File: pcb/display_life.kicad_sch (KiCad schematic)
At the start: 45 parts, among them J3 1st Bit_shifter, J4 1st 7 Segment, Q1 Q_NPN_CBE, Q2 Q_NPN_CBE, Q3 Q_NPN_CBE, Q4 Q_NPN_CBE, Q5 Q_NPN_CBE, Q6 Q_NPN_CBE, Q7 Q_NPN_CBE, Q8 Q_NPN_CBE, U2 74HC595, U3 74HC595, U4 4028, U5 CC56-12SURKWA, U6 CC56-12SURKWA

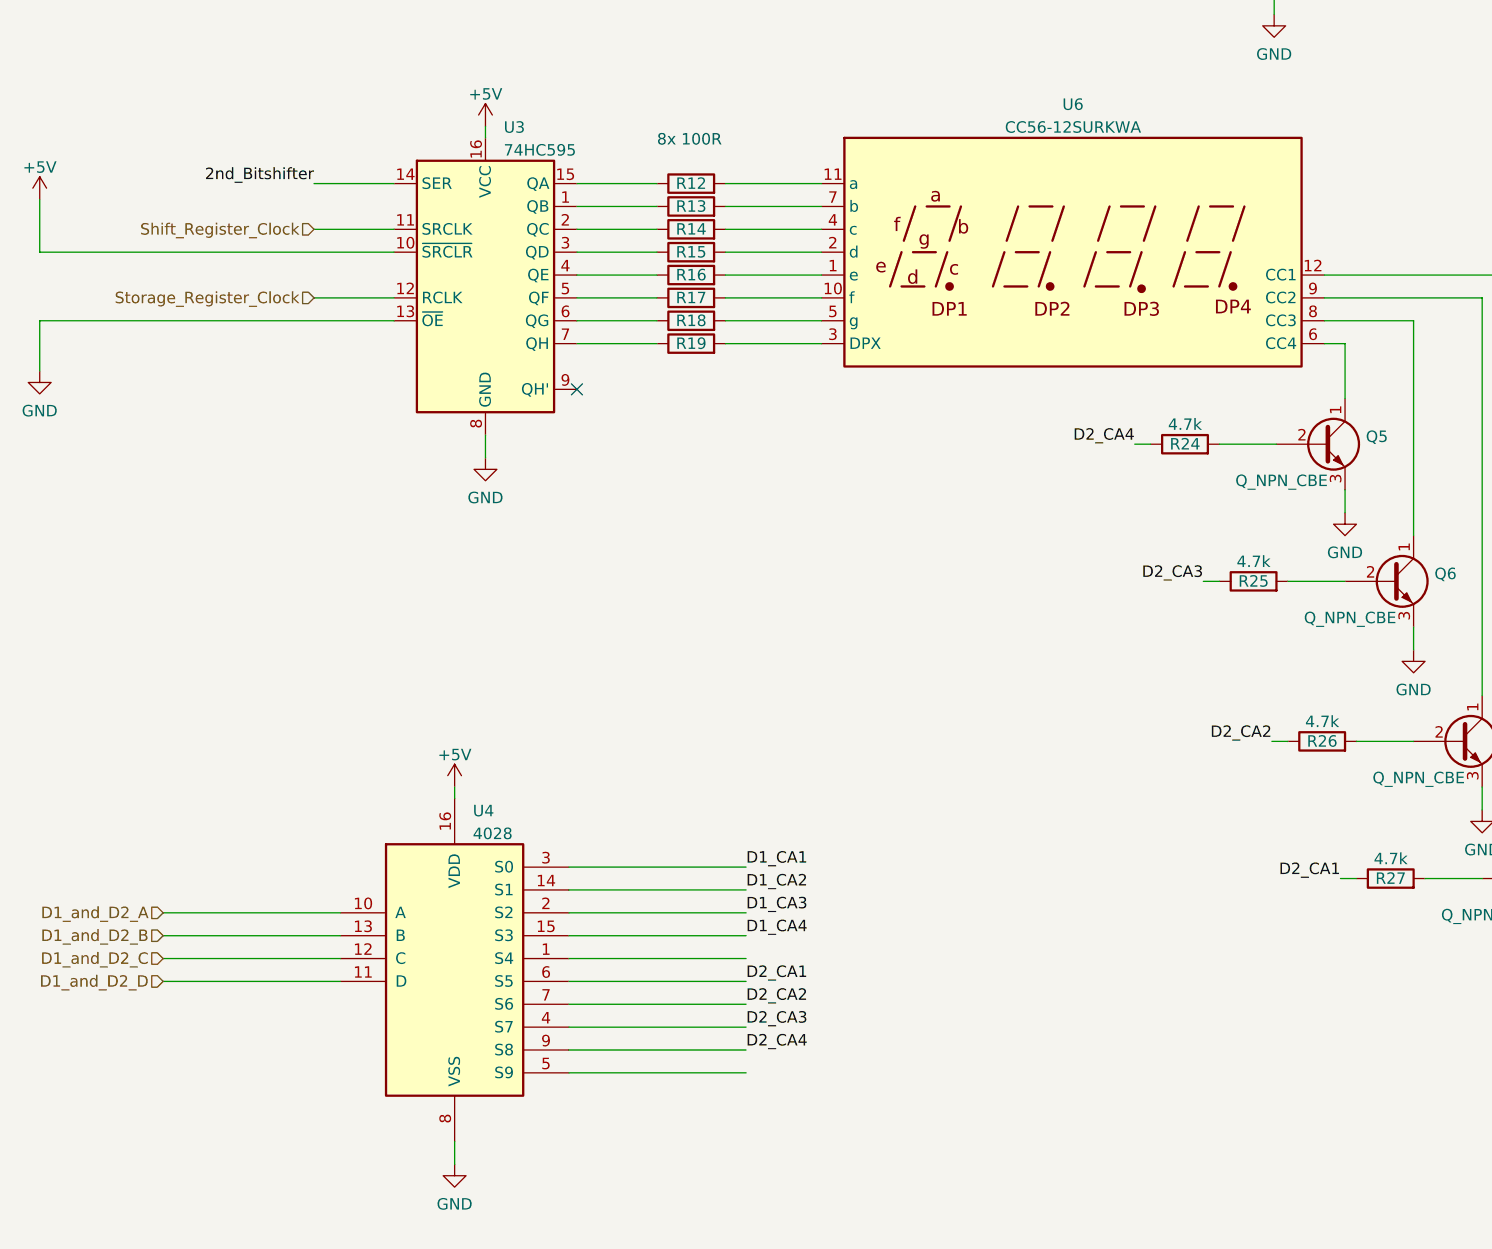
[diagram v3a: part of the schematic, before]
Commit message: reduced to 2 displays and logig analyzer output added
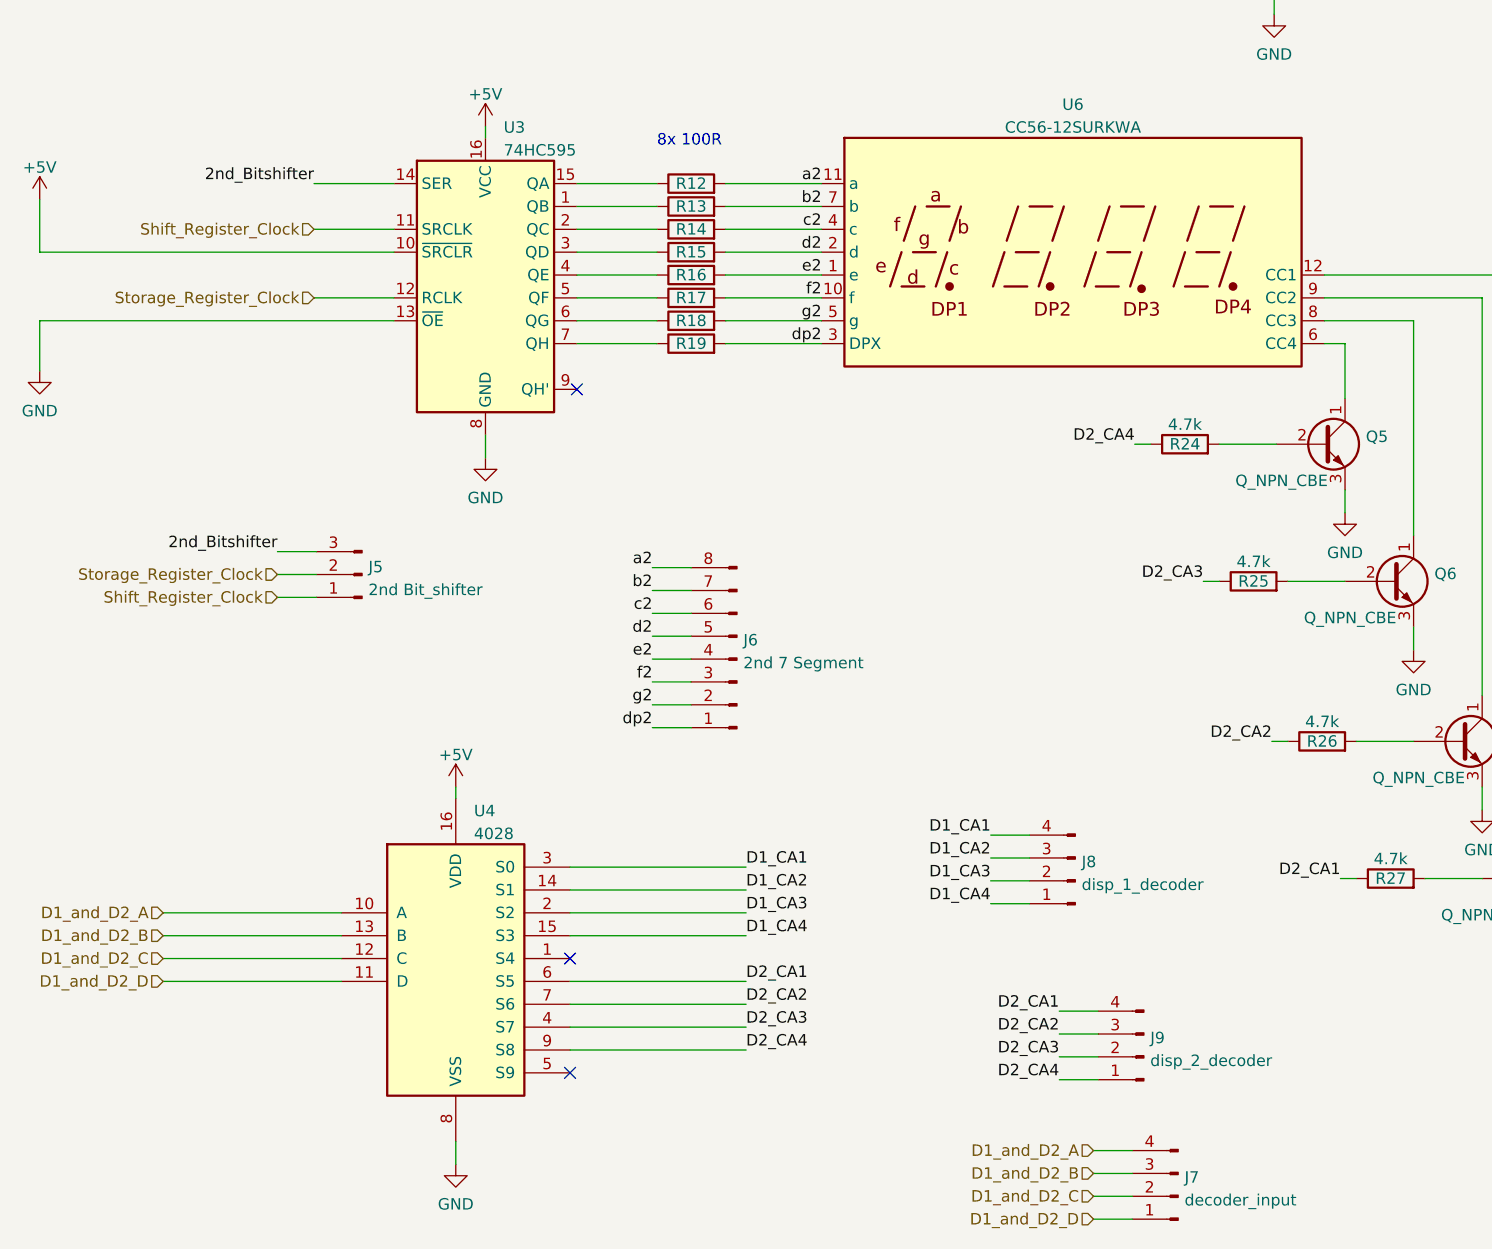
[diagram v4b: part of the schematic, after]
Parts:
- added J5: 2nd Bit_shifter, Connector_PinHeader_2.54mm:PinHeader_1x03_P2.54mm_Vertical, symbol Connector:Conn_01x03_Male
- added J6: 2nd 7 Segment, Connector_PinHeader_2.54mm:PinHeader_1x08_P2.54mm_Vertical, symbol Connector:Conn_01x08_Male
- added J7: decoder_input, Connector_PinHeader_2.54mm:PinHeader_1x04_P2.54mm_Vertical, symbol Connector:Conn_01x04_Male
- added J8: disp_1_decoder, Connector_PinHeader_2.54mm:PinHeader_1x04_P2.54mm_Vertical, symbol Connector:Conn_01x04_Male
- added J9: disp_2_decoder, Connector_PinHeader_2.54mm:PinHeader_1x04_P2.54mm_Vertical, symbol Connector:Conn_01x04_Male
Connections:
- net 2nd_Bitshifter: now also J5.3 (Pin_3)
- net D1_CA1: now also J8.4 (Pin_4)
- net D1_CA2: now also J8.3 (Pin_3)
- net D1_CA3: now also J8.2 (Pin_2)
- net D1_CA4: now also J8.1 (Pin_1)
- net D1_and_D2_A: now also J7.4 (Pin_4)
- net D1_and_D2_B: now also J7.3 (Pin_3)
- net D1_and_D2_C: now also J7.2 (Pin_2)
- net D1_and_D2_D: now also J7.1 (Pin_1)
- net D2_CA1: now also J9.4 (Pin_4)
- net D2_CA2: now also J9.3 (Pin_3)
- net D2_CA3: now also J9.2 (Pin_2)
- net D2_CA4: now also J9.1 (Pin_1)
- net Shift_Register_Clock: now also J5.1 (Pin_1)
- net Storage_Register_Clock: now also J5.2 (Pin_2)
- net e2: now reaches R16.2, U6.1 (e)
- net e2: now also J6.4 (Pin_4)
- net c2: now reaches R14.2, U6.4 (c)
- net c2: now also J6.6 (Pin_6)
- net a2: now reaches R12.2, U6.11 (a)
- net a2: now also J6.8 (Pin_8)
- net b2: now reaches R13.2, U6.7 (b)
- net b2: now also J6.7 (Pin_7)
- net f2: now reaches R17.2, U6.10 (f)
- net f2: now also J6.3 (Pin_3)
- net d2: now reaches R15.2, U6.2 (d)
- net d2: now also J6.5 (Pin_5)
- net dp2: now reaches R19.2, U6.3 (DPX)
- net dp2: now also J6.1 (Pin_1)
- net g2: now reaches R18.2, U6.5 (g)
- net g2: now also J6.2 (Pin_2)
- no-connect marks 1 -> 3

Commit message: new parts and stuff
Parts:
- removed J4: 1st 7 Segment, Connector_PinHeader_2.54mm:PinHeader_1x08_P2.54mm_Vertical, symbol Connector:Conn_01x08_Male
- removed J6: 2nd 7 Segment, Connector_PinHeader_2.54mm:PinHeader_1x08_P2.54mm_Vertical, symbol Connector:Conn_01x08_Male
- added J4: 1st 7 Segment, Connector_PinHeader_2.54mm:PinHeader_1x10_P2.54mm_Vertical, symbol Connector:Conn_01x10_Female
- added J6: 2nd 7 Segment, Connector_PinHeader_2.54mm:PinHeader_1x10_P2.54mm_Vertical, symbol Connector:Conn_01x10_Female
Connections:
- net +5V: now also J4.1 (Pin_1), J6.1 (Pin_1)
- net GND: now also J4.10 (Pin_10), J6.10 (Pin_10)
- net a1: now also J4.2 (Pin_2)
- net a2: now also J6.2 (Pin_2)
- net b1: now also J4.3 (Pin_3)
- net b2: now also J6.3 (Pin_3)
- net c1: now also J4.4 (Pin_4)
- net c2: now also J6.4 (Pin_4)
- net d1: now also J4.5 (Pin_5)
- net d2: now also J6.5 (Pin_5)
- net dp1: now also J4.9 (Pin_9)
- net dp2: now also J6.9 (Pin_9)
- net e1: now also J4.6 (Pin_6)
- net e2: now also J6.6 (Pin_6)
- net f1: now also J4.7 (Pin_7)
- net f2: now also J6.7 (Pin_7)
- net g1: now also J4.8 (Pin_8)
- net g2: now also J6.8 (Pin_8)
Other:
- note added: "Debug Pins"
- moved on the sheet: J3, J5, J7, J8, J9, U4

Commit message: new layout with usb
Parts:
- R10, R11, R12, R13, R14, R15, R16, R17, R18, R19, R20, R21, R22, R23, R24, R25, R26, R27, R4, R5, R6, R7, R8, R9: footprint Resistor_THT:R_Axial_DIN0207_L6.3mm_D2.5mm_P7.62mm_Horizontal -> Resistor_THT:R_Axial_DIN0207_L6.3mm_D2.5mm_P10.16mm_Horizontal
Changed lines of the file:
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@@
       (effects (font (size 1.27 1.27)) hide)
     )
-    (property "Footprint" "Resistor_THT:R_Axial_DIN0207_L6.3mm_D2.5mm_P7.62mm_Horizontal" (id 2) (at 94.488 87.884 90)
+    (property "Footprint" "Resistor_THT:R_Axial_DIN0207_L6.3mm_D2.5mm_P10.16mm_Horizontal" (id 2) (at 94.488 87.884 90)
       (effects (font (size 1.27 1.27)) hide)
     )
@@
     (property "Reference" "R21" (id 0) (at 244.602 70.866 90))
     (property "Value" "4.7k" (id 1) (at 244.602 68.6871 90))
-    (property "Footprint" "Resistor_THT:R_Axial_DIN0207_L6.3mm_D2.5mm_P7.62mm_Horizontal" (id 2) (at 244.602 72.644 90)
+    (property "Footprint" "Resistor_THT:R_Axial_DIN0207_L6.3mm_D2.5mm_P10.16mm_Horizontal" (id 2) (at 244.602 72.644 90)
       (effects (font (size 1.27 1.27)) hide)
     )
@@
     (property "Reference" "R20" (id 0) (at 236.982 55.626 90))
     (property "Value" "4.7k" (id 1) (at 236.982 53.4471 90))
-    (property "Footprint" "Resistor_THT:R_Axial_DIN0207_L6.3mm_D2.5mm_P7.62mm_Horizontal" (id 2) (at 236.982 57.404 90)
+    (property "Footprint" "Resistor_THT:R_Axial_DIN0207_L6.3mm_D2.5mm_P10.16mm_Horizontal" (id 2) (at 236.982 57.404 90)
       (effects (font (size 1.27 1.27)) hide)
     )
@@
       (effects (font (size 1.27 1.27)) hide)
     )
-    (property "Footprint" "Resistor_THT:R_Axial_DIN0207_L6.3mm_D2.5mm_P7.62mm_Horizontal" (id 2) (at 94.488 82.804 90)
+    (property "Footprint" "Resistor_THT:R_Axial_DIN0207_L6.3mm_D2.5mm_P10.16mm_Horizontal" (id 2) (at 94.488 82.804 90)
       (effects (font (size 1.27 1.27)) hide)
     )
@@
     (property "Reference" "R24" (id 0) (at 149.352 104.902 90))
     (property "Value" "4.7k" (id 1) (at 149.352 102.7231 90))
-    (property "Footprint" "Resistor_THT:R_Axial_DIN0207_L6.3mm_D2.5mm_P7.62mm_Horizontal" (id 2) (at 149.352 106.68 90)
+    (property "Footprint" "Resistor_THT:R_Axial_DIN0207_L6.3mm_D2.5mm_P10.16mm_Horizontal" (id 2) (at 149.352 106.68 90)
       (effects (font (size 1.27 1.27)) hide)
     )
@@
       (effects (font (size 1.27 1.27)) hide)
     )
-    (property "Footprint" "Resistor_THT:R_Axial_DIN0207_L6.3mm_D2.5mm_P7.62mm_Horizontal" (id 2) (at 182.118 30.988 90)
+    (property "Footprint" "Resistor_THT:R_Axial_DIN0207_L6.3mm_D2.5mm_P10.16mm_Horizontal" (id 2) (at 182.118 30.988 90)
       (effects (font (size 1.27 1.27)) hide)
     )
@@
     (property "Reference" "R23" (id 0) (at 259.842 103.886 90))
     (property "Value" "4.7k" (id 1) (at 259.842 101.7071 90))
-    (property "Footprint" "Resistor_THT:R_Axial_DIN0207_L6.3mm_D2.5mm_P7.62mm_Horizontal" (id 2) (at 259.842 105.664 90)
+    (property "Footprint" "Resistor_THT:R_Axial_DIN0207_L6.3mm_D2.5mm_P10.16mm_Horizontal" (id 2) (at 259.842 105.664 90)
       (effects (font (size 1.27 1.27)) hide)
     )
@@
     (property "Reference" "R25" (id 0) (at 156.972 120.142 90))
     (property "Value" "4.7k" (id 1) (at 156.972 117.9631 90))
-    (property "Footprint" "Resistor_THT:R_Axial_DIN0207_L6.3mm_D2.5mm_P7.62mm_Horizontal" (id 2) (at 156.972 121.92 90)
+    (property "Footprint" "Resistor_THT:R_Axial_DIN0207_L6.3mm_D2.5mm_P10.16mm_Horizontal" (id 2) (at 156.972 121.92 90)
       (effects (font (size 1.27 1.27)) hide)
     )
@@
       (effects (font (size 1.27 1.27)) hide)
     )
-    (property "Footprint" "Resistor_THT:R_Axial_DIN0207_L6.3mm_D2.5mm_P7.62mm_Horizontal" (id 2) (at 182.118 46.228 90)
+    (property "Footprint" "Resistor_THT:R_Axial_DIN0207_L6.3mm_D2.5mm_P10.16mm_Horizontal" (id 2) (at 182.118 46.228 90)
       (effects (font (size 1.27 1.27)) hide)
     )
@@
     (property "Reference" "R26" (id 0) (at 164.592 137.922 90))
     (property "Value" "4.7k" (id 1) (at 164.592 135.7431 90))
-    (property "Footprint" "Resistor_THT:R_Axial_DIN0207_L6.3mm_D2.5mm_P7.62mm_Horizontal" (id 2) (at 164.592 139.7 90)
+    (property "Footprint" "Resistor_THT:R_Axial_DIN0207_L6.3mm_D2.5mm_P10.16mm_Horizontal" (id 2) (at 164.592 139.7 90)
       (effects (font (size 1.27 1.27)) hide)
     )
@@
       (effects (font (size 1.27 1.27)) hide)
     )
-    (property "Footprint" "Resistor_THT:R_Axial_DIN0207_L6.3mm_D2.5mm_P7.62mm_Horizontal" (id 2) (at 182.118 36.068 90)
+    (property "Footprint" "Resistor_THT:R_Axial_DIN0207_L6.3mm_D2.5mm_P10.16mm_Horizontal" (id 2) (at 182.118 36.068 90)
       (effects (font (size 1.27 1.27)) hide)
     )
@@
       (effects (font (size 1.27 1.27)) hide)
     )
-    (property "Footprint" "Resistor_THT:R_Axial_DIN0207_L6.3mm_D2.5mm_P7.62mm_Horizontal" (id 2) (at 94.488 77.724 90)
+    (property "Footprint" "Resistor_THT:R_Axial_DIN0207_L6.3mm_D2.5mm_P10.16mm_Horizontal" (id 2) (at 94.488 77.724 90)
       (effects (font (size 1.27 1.27)) hide)
     )
@@
       (effects (font (size 1.27 1.27)) hide)
     )
-    (property "Footprint" "Resistor_THT:R_Axial_DIN0207_L6.3mm_D2.5mm_P7.62mm_Horizontal" (id 2) (at 94.488 80.264 90)
+    (property "Footprint" "Resistor_THT:R_Axial_DIN0207_L6.3mm_D2.5mm_P10.16mm_Horizontal" (id 2) (at 94.488 80.264 90)
       (effects (font (size 1.27 1.27)) hide)
     )
@@
       (effects (font (size 1.27 1.27)) hide)
     )
-    (property "Footprint" "Resistor_THT:R_Axial_DIN0207_L6.3mm_D2.5mm_P7.62mm_Horizontal" (id 2) (at 94.488 90.424 90)
+    (property "Footprint" "Resistor_THT:R_Axial_DIN0207_L6.3mm_D2.5mm_P10.16mm_Horizontal" (id 2) (at 94.488 90.424 90)
       (effects (font (size 1.27 1.27)) hide)
     )
@@
       (effects (font (size 1.27 1.27)) hide)
     )
-    (property "Footprint" "Resistor_THT:R_Axial_DIN0207_L6.3mm_D2.5mm_P7.62mm_Horizontal" (id 2) (at 94.488 85.344 90)
+    (property "Footprint" "Resistor_THT:R_Axial_DIN0207_L6.3mm_D2.5mm_P10.16mm_Horizontal" (id 2) (at 94.488 85.344 90)
       (effects (font (size 1.27 1.27)) hide)
     )
@@
       (effects (font (size 1.27 1.27)) hide)
     )
-    (property "Footprint" "Resistor_THT:R_Axial_DIN0207_L6.3mm_D2.5mm_P7.62mm_Horizontal" (id 2) (at 182.118 41.148 90)
+    (property "Footprint" "Resistor_THT:R_Axial_DIN0207_L6.3mm_D2.5mm_P10.16mm_Horizontal" (id 2) (at 182.118 41.148 90)
       (effects (font (size 1.27 1.27)) hide)
     )
@@
       (effects (font (size 1.27 1.27)) hide)
     )
-    (property "Footprint" "Resistor_THT:R_Axial_DIN0207_L6.3mm_D2.5mm_P7.62mm_Horizontal" (id 2) (at 94.488 92.964 90)
+    (property "Footprint" "Resistor_THT:R_Axial_DIN0207_L6.3mm_D2.5mm_P10.16mm_Horizontal" (id 2) (at 94.488 92.964 90)
       (effects (font (size 1.27 1.27)) hide)
     )
@@
       (effects (font (size 1.27 1.27)) hide)
     )
-    (property "Footprint" "Resistor_THT:R_Axial_DIN0207_L6.3mm_D2.5mm_P7.62mm_Horizontal" (id 2) (at 182.118 28.448 90)
+    (property "Footprint" "Resistor_THT:R_Axial_DIN0207_L6.3mm_D2.5mm_P10.16mm_Horizontal" (id 2) (at 182.118 28.448 90)
       (effects (font (size 1.27 1.27)) hide)
     )
@@
       (effects (font (size 1.27 1.27)) hide)
     )
-    (property "Footprint" "Resistor_THT:R_Axial_DIN0207_L6.3mm_D2.5mm_P7.62mm_Horizontal" (id 2) (at 182.118 38.608 90)
+    (property "Footprint" "Resistor_THT:R_Axial_DIN0207_L6.3mm_D2.5mm_P10.16mm_Horizontal" (id 2) (at 182.118 38.608 90)
       (effects (font (size 1.27 1.27)) hide)
     )
@@
       (effects (font (size 1.27 1.27)) hide)
     )
-    (property "Footprint" "Resistor_THT:R_Axial_DIN0207_L6.3mm_D2.5mm_P7.62mm_Horizontal" (id 2) (at 182.118 43.688 90)
+    (property "Footprint" "Resistor_THT:R_Axial_DIN0207_L6.3mm_D2.5mm_P10.16mm_Horizontal" (id 2) (at 182.118 43.688 90)
       (effects (font (size 1.27 1.27)) hide)
     )
@@
       (effects (font (size 1.27 1.27)) hide)
     )
-    (property "Footprint" "Resistor_THT:R_Axial_DIN0207_L6.3mm_D2.5mm_P7.62mm_Horizontal" (id 2) (at 182.118 33.528 90)
+    (property "Footprint" "Resistor_THT:R_Axial_DIN0207_L6.3mm_D2.5mm_P10.16mm_Horizontal" (id 2) (at 182.118 33.528 90)
       (effects (font (size 1.27 1.27)) hide)
     )
@@
     (property "Reference" "R27" (id 0) (at 172.212 153.162 90))
     (property "Value" "4.7k" (id 1) (at 172.212 150.9831 90))
-    (property "Footprint" "Resistor_THT:R_Axial_DIN0207_L6.3mm_D2.5mm_P7.62mm_Horizontal" (id 2) (at 172.212 154.94 90)
+    (property "Footprint" "Resistor_THT:R_Axial_DIN0207_L6.3mm_D2.5mm_P10.16mm_Horizontal" (id 2) (at 172.212 154.94 90)
       (effects (font (size 1.27 1.27)) hide)
     )
@@
       (effects (font (size 1.27 1.27)) hide)
     )
-    (property "Footprint" "Resistor_THT:R_Axial_DIN0207_L6.3mm_D2.5mm_P7.62mm_Horizontal" (id 2) (at 94.488 95.504 90)
+    (property "Footprint" "Resistor_THT:R_Axial_DIN0207_L6.3mm_D2.5mm_P10.16mm_Horizontal" (id 2) (at 94.488 95.504 90)
       (effects (font (size 1.27 1.27)) hide)
     )
@@
     (property "Reference" "R22" (id 0) (at 252.222 88.646 90))
     (property "Value" "4.7k" (id 1) (at 252.222 86.4671 90))
-    (property "Footprint" "Resistor_THT:R_Axial_DIN0207_L6.3mm_D2.5mm_P7.62mm_Horizontal" (id 2) (at 252.222 90.424 90)
-      (effects (font (size 1.27 1.27)) hide)
-    )
+    (property "Footprint" "Resistor_THT:R_Axial_DIN0207_L6.3mm_D2.5mm_P10.16mm_Horizontal" (id 2) (at 252.222 90.424 90)
+      (effects (font (size 1.27 1.27)) hide)
+    )
